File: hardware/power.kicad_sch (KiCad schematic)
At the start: 16 parts

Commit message: MCU module is completed
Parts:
- C1: value (none) -> 10uF/10V; footprint (none) -> Capacitor_SMD:CP_Elec_6.3x7.7
- C2, C6: value (none) -> 100uF/35V; footprint (none) -> Capacitor_SMD:CP_Elec_10x10.5
- C3, C4: value (none) -> 10nF; footprint (none) -> Capacitor_SMD:C_0603_1608Metric
- C5: value (none) -> 10uF/35V; footprint (none) -> Capacitor_SMD:CP_Elec_6.3x7.7
- D1: value (none) -> SBR3A40SAQ; footprint (none) -> Diode_SMD:D_SMB_Handsoldering
- F1: value (none) -> 1A; footprint (none) -> Fuse:Fuse_1206_3216Metric
- R1: value (none) -> 470; footprint (none) -> Resistor_SMD:R_0603_1608Metric
- R2: value (none) -> 18K; footprint (none) -> Resistor_SMD:R_0603_1608Metric
- R3: value (none) -> 10K; footprint (none) -> Resistor_SMD:R_0603_1608Metric
- R4: value (none) -> 1K; footprint (none) -> Resistor_SMD:R_0603_1608Metric
- R5: value (none) -> 33; footprint (none) -> Resistor_SMD:R_0603_1608Metric
- R6: value (none) -> 120; footprint (none) -> Resistor_SMD:R_0603_1608Metric
- U1: value (none) -> TPS7A4901DGNT; footprint (none) -> TPS7A4901DGNT:SOP65P490X110-9N
- U2: value (none) -> LD1085D2M-R; footprint (none) -> LD1085D2MR:LD1085D2M-R
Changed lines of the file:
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@@
       (effects (font (size 1.27 1.27)) (justify left))
     )
-    (property "Value" "" (id 1) (at 128.27 55.88 0)
-      (effects (font (size 1.27 1.27)) (justify left))
-    )
-    (property "Footprint" "" (id 2) (at 127.9652 57.15 0)
+    (property "Value" "100uF/35V" (id 1) (at 128.27 55.88 0)
+      (effects (font (size 1.27 1.27)) (justify left))
+    )
+    (property "Footprint" "Capacitor_SMD:CP_Elec_10x10.5" (id 2) (at 127.9652 57.15 0)
       (effects (font (size 1.27 1.27)) hide)
     )
@@
     (in_bom yes) (on_board yes)
     (property "Reference" "D1" (id 0) (at 115.57 41.91 0))
-    (property "Value" "" (id 1) (at 116.84 46.99 0))
-    (property "Footprint" "" (id 2) (at 115.57 44.45 0)
+    (property "Value" "SBR3A40SAQ" (id 1) (at 116.84 46.99 0))
+    (property "Footprint" "Diode_SMD:D_SMB_Handsoldering" (id 2) (at 115.57 44.45 0)
       (effects (font (size 1.27 1.27)) hide)
     )
@@
     (in_bom yes) (on_board yes)
     (property "Reference" "F1" (id 0) (at 101.6 41.91 90))
-    (property "Value" "" (id 1) (at 101.6 46.99 90))
-    (property "Footprint" "" (id 2) (at 101.6 42.672 90)
+    (property "Value" "1A" (id 1) (at 101.6 46.99 90))
+    (property "Footprint" "Fuse:Fuse_1206_3216Metric" (id 2) (at 101.6 42.672 90)
       (effects (font (size 1.27 1.27)) hide)
     )
@@
       (effects (font (size 1.27 1.27)) (justify left))
     )
-    (property "Value" "" (id 1) (at 199.898 51.943 0)
-      (effects (font (size 1.27 1.27)) (justify left))
-    )
-    (property "Footprint" "" (id 2) (at 196.342 50.8 90)
+    (property "Value" "120" (id 1) (at 199.898 51.943 0)
+      (effects (font (size 1.27 1.27)) (justify left))
+    )
+    (property "Footprint" "Resistor_SMD:R_0603_1608Metric" (id 2) (at 196.342 50.8 90)
       (effects (font (size 1.27 1.27)) hide)
     )
@@
       (effects (font (size 1.27 1.27)) (justify left))
     )
-    (property "Value" "" (id 1) (at 189.738 64.643 0)
-      (effects (font (size 1.27 1.27)) (justify left))
-    )
-    (property "Footprint" "" (id 2) (at 186.182 63.5 90)
+    (property "Value" "1K" (id 1) (at 189.738 64.643 0)
+      (effects (font (size 1.27 1.27)) (justify left))
+    )
+    (property "Footprint" "Resistor_SMD:R_0603_1608Metric" (id 2) (at 186.182 63.5 90)
       (effects (font (size 1.27 1.27)) hide)
     )
@@
       (effects (font (size 1.27 1.27)) (justify left))
     )
-    (property "Value" "" (id 1) (at 210.82 53.34 0)
-      (effects (font (size 1.27 1.27)) (justify left))
-    )
-    (property "Footprint" "" (id 2) (at 211.7852 54.61 0)
+    (property "Value" "100uF/35V" (id 1) (at 210.82 53.34 0)
+      (effects (font (size 1.27 1.27)) (justify left))
+    )
+    (property "Footprint" "Capacitor_SMD:CP_Elec_10x10.5" (id 2) (at 211.7852 54.61 0)
       (effects (font (size 1.27 1.27)) hide)
     )
@@
       (effects (font (size 1.27 1.27)) hide)
     )
-    (property "Value" "" (id 1) (at 188.087 84.4042 0))
+    (property "Value" "GND" (id 1) (at 188.087 84.4042 0))
     (property "Footprint" "" (id 2) (at 187.96 80.01 0)
       (effects (font (size 1.27 1.27)) hide)
@@
     (in_bom yes) (on_board yes)
     (property "Reference" "U1" (id 0) (at 165.1 102.362 0))
-    (property "Value" "" (id 1) (at 165.1 104.6734 0))
-    (property "Footprint" "" (id 2) (at 165.1 119.38 0)
+    (property "Value" "TPS7A4901DGNT" (id 1) (at 165.1 104.6734 0))
+    (property "Footprint" "TPS7A4901DGNT:SOP65P490X110-9N" (id 2) (at 165.1 119.38 0)
       (effects (font (size 1.27 1.27)) (justify left bottom) hide)
     )
@@
       (effects (font (size 1.27 1.27)) (justify left))
     )
-    (property "Value" "" (id 1) (at 142.24 124.46 0)
-      (effects (font (size 1.27 1.27)) (justify left))
-    )
-    (property "Footprint" "" (id 2) (at 141.9352 125.73 0)
+    (property "Value" "10nF" (id 1) (at 142.24 124.46 0)
+      (effects (font (size 1.27 1.27)) (justify left))
+    )
+    (property "Footprint" "Capacitor_SMD:C_0603_1608Metric" (id 2) (at 141.9352 125.73 0)
       (effects (font (size 1.27 1.27)) hide)
     )
@@
       (effects (font (size 1.27 1.27)) (justify left))
     )
-    (property "Value" "" (id 1) (at 204.47 123.19 0)
-      (effects (font (size 1.27 1.27)) (justify left))
-    )
-    (property "Footprint" "" (id 2) (at 204.1652 124.46 0)
+    (property "Value" "10uF/35V" (id 1) (at 204.47 123.19 0)
+      (effects (font (size 1.27 1.27)) (justify left))
+    )
+    (property "Footprint" "Capacitor_SMD:CP_Elec_6.3x7.7" (id 2) (at 204.1652 124.46 0)
       (effects (font (size 1.27 1.27)) hide)
     )
@@
       (effects (font (size 1.27 1.27)) hide)
     )
-    (property "Value" "" (id 1) (at 203.327 132.6642 0))
+    (property "Value" "GND" (id 1) (at 203.327 132.6642 0))
     (property "Footprint" "" (id 2) (at 203.2 128.27 0)
       (effects (font (size 1.27 1.27)) hide)
@@
       (effects (font (size 1.27 1.27)) hide)
     )
-    (property "Value" "" (id 1) (at 185.547 154.2542 0))
+    (property "Value" "GND" (id 1) (at 185.547 154.2542 0))
     (property "Footprint" "" (id 2) (at 185.42 149.86 0)
       (effects (font (size 1.27 1.27)) hide)
@@
       (effects (font (size 1.27 1.27)) hide)
     )
-    (property "Value" "" (id 1) (at 104.521 103.5558 0))
+    (property "Value" "+3V3" (id 1) (at 104.521 103.5558 0))
     (property "Footprint" "" (id 2) (at 104.14 107.95 0)
       (effects (font (size 1.27 1.27)) hide)
@@
       (effects (font (size 1.27 1.27)) (justify left))
     )
-    (property "Value" "" (id 1) (at 132.08 124.46 0)
-      (effects (font (size 1.27 1.27)) (justify left))
-    )
-    (property "Footprint" "" (id 2) (at 131.7752 125.73 0)
+    (property "Value" "10nF" (id 1) (at 132.08 124.46 0)
+      (effects (font (size 1.27 1.27)) (justify left))
+    )
+    (property "Footprint" "Capacitor_SMD:C_0603_1608Metric" (id 2) (at 131.7752 125.73 0)
       (effects (font (size 1.27 1.27)) hide)
     )
@@
       (effects (font (size 1.27 1.27)) (justify left))
     )
-    (property "Value" "" (id 1) (at 118.618 123.063 0)
-      (effects (font (size 1.27 1.27)) (justify left))
-    )
-    (property "Footprint" "" (id 2) (at 115.062 121.92 90)
+    (property "Value" "18K" (id 1) (at 118.618 123.063 0)
+      (effects (font (size 1.27 1.27)) (justify left))
+    )
+    (property "Footprint" "Resistor_SMD:R_0603_1608Metric" (id 2) (at 115.062 121.92 90)
       (effects (font (size 1.27 1.27)) hide)
     )
@@
       (effects (font (size 1.27 1.27)) (justify left))
     )
-    (property "Value" "" (id 1) (at 118.618 139.573 0)
-      (effects (font (size 1.27 1.27)) (justify left))
-    )
-    (property "Footprint" "" (id 2) (at 115.062 138.43 90)
+    (property "Value" "10K" (id 1) (at 118.618 139.573 0)
+      (effects (font (size 1.27 1.27)) (justify left))
+    )
+    (property "Footprint" "Resistor_SMD:R_0603_1608Metric" (id 2) (at 115.062 138.43 90)
       (effects (font (size 1.27 1.27)) hide)
     )
@@
       (effects (font (size 1.27 1.27)) (justify left))
     )
-    (property "Value" "" (id 1) (at 105.41 132.08 0)
-      (effects (font (size 1.27 1.27)) (justify left))
-    )
-    (property "Footprint" "" (id 2) (at 105.1052 133.35 0)
+    (property "Value" "10uF/10V" (id 1) (at 105.41 132.08 0)
+      (effects (font (size 1.27 1.27)) (justify left))
+    )
+    (property "Footprint" "Capacitor_SMD:CP_Elec_6.3x7.7" (id 2) (at 105.1052 133.35 0)
       (effects (font (size 1.27 1.27)) hide)
     )
@@
       (effects (font (size 1.27 1.27)) hide)
     )
-    (property "Value" "" (id 1) (at 127.127 66.6242 0))
+    (property "Value" "GND" (id 1) (at 127.127 66.6242 0))
     (property "Footprint" "" (id 2) (at 127 62.23 0)
       (effects (font (size 1.27 1.27)) hide)
@@
       (effects (font (size 1.27 1.27)) hide)
     )
-    (property "Value" "" (id 1) (at 226.441 32.4358 0))
+    (property "Value" "+12V" (id 1) (at 226.441 32.4358 0))
     (property "Footprint" "" (id 2) (at 226.06 36.83 0)
       (effects (font (size 1.27 1.27)) hide)
@@
       (effects (font (size 1.27 1.27)) hide)
     )
-    (property "Value" "" (id 1) (at 91.821 32.4358 0))
+    (property "Value" "VCC" (id 1) (at 91.821 32.4358 0))
     (property "Footprint" "" (id 2) (at 91.44 36.83 0)
       (effects (font (size 1.27 1.27)) hide)
@@
       (effects (font (size 1.524 1.524)))
     )
-    (property "Value" "" (id 1) (at 157.48 52.07 0)
+    (property "Value" "LD1085D2M-R" (id 1) (at 157.48 52.07 0)
       (effects (font (size 1.524 1.524)))
     )
-    (property "Footprint" "" (id 2) (at 157.48 35.814 0)
+    (property "Footprint" "LD1085D2MR:LD1085D2M-R" (id 2) (at 157.48 35.814 0)
       (effects (font (size 1.524 1.524)) hide)
     )
@@
       (effects (font (size 1.27 1.27)) hide)
     )
-    (property "Value" "" (id 1) (at 210.947 64.0842 0))
+    (property "Value" "GND" (id 1) (at 210.947 64.0842 0))
     (property "Footprint" "" (id 2) (at 210.82 59.69 0)
       (effects (font (size 1.27 1.27)) hide)
@@
       (effects (font (size 1.27 1.27)) (justify left))
     )
-    (property "Value" "" (id 1) (at 189.738 74.803 0)
-      (effects (font (size 1.27 1.27)) (justify left))
-    )
-    (property "Footprint" "" (id 2) (at 186.182 73.66 90)
+    (property "Value" "33" (id 1) (at 189.738 74.803 0)
+      (effects (font (size 1.27 1.27)) (justify left))
+    )
+    (property "Footprint" "Resistor_SMD:R_0603_1608Metric" (id 2) (at 186.182 73.66 90)
       (effects (font (size 1.27 1.27)) hide)
     )
@@
     (in_bom yes) (on_board yes)
     (property "Reference" "R1" (id 0) (at 97.79 109.22 90))
-    (property "Value" "" (id 1) (at 97.79 114.3 90))
-    (property "Footprint" "" (id 2) (at 97.79 109.982 90)
-      (effects (font (size 1.27 1.27)) hide)
-    )
+    (property "Value" "470" (id 1) (at 97.79 114.3 90))
+    (property "Footprint" "Resistor_SMD:R_0603_1608Metric" (id 2) (at 97.79 109.982 90)
+      (effects (font (size 1.27 1.27)) hide)
+    )

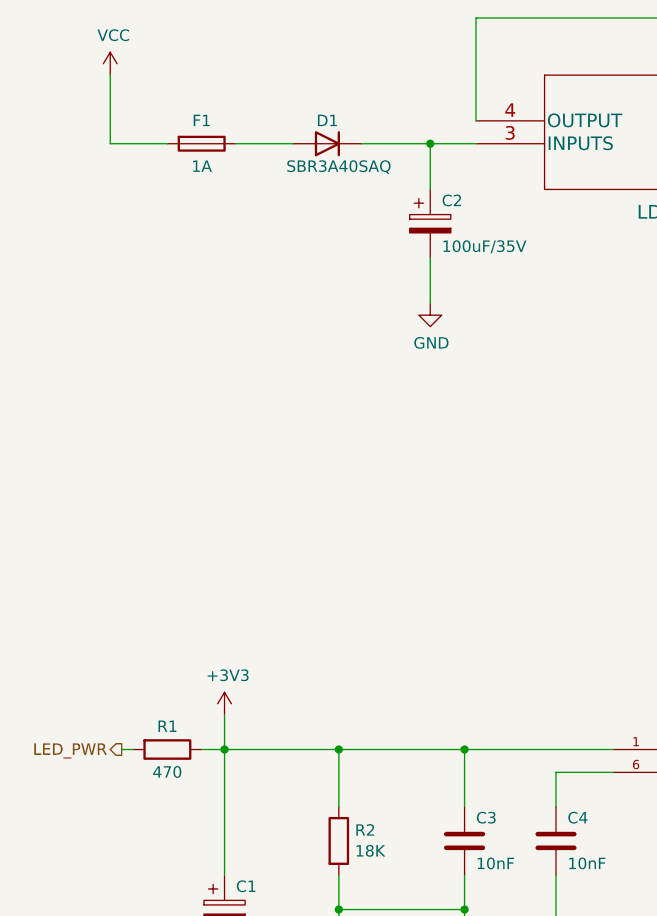
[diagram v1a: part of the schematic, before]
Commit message: Relay module completed
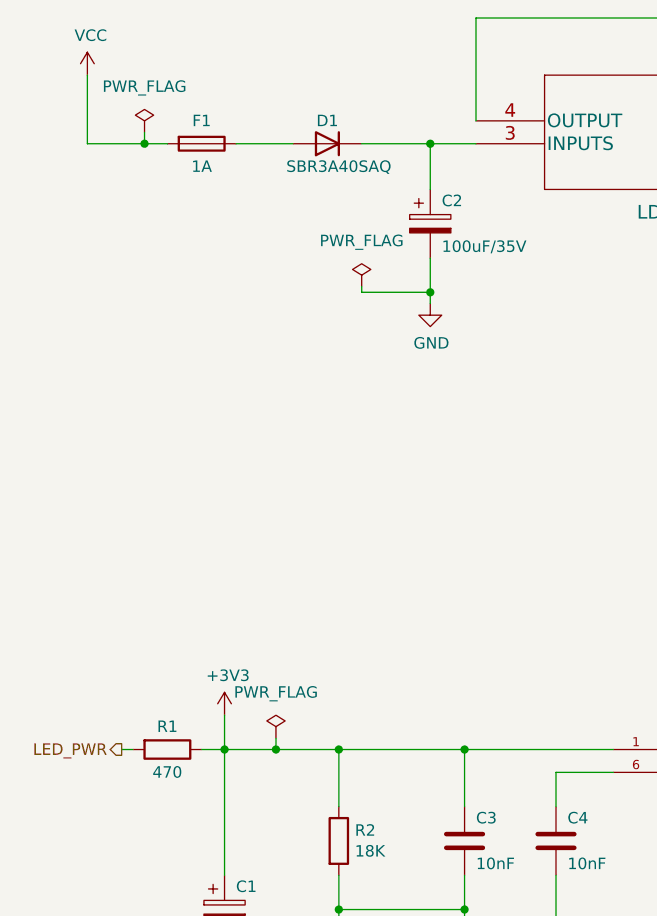
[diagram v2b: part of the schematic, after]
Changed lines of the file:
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@@
   (junction (at 203.2 111.76) (diameter 0) (color 0 0 0 0)
   )
+  (junction (at 95.25 44.45) (diameter 0) (color 0 0 0 0)
+  )
   (junction (at 185.42 111.76) (diameter 0) (color 0 0 0 0)
   )
@@
   (junction (at 104.14 111.76) (diameter 0) (color 0 0 0 0)
   )
+  (junction (at 109.855 111.76) (diameter 0) (color 0 0 0 0)
+  )
   (junction (at 140.97 147.32) (diameter 0) (color 0 0 0 0)
   )
@@
   (junction (at 116.84 111.76) (diameter 0) (color 0 0 0 0)
   )
+  (junction (at 127 60.96) (diameter 0) (color 0 0 0 0)
+  )
   (junction (at 198.12 44.45) (diameter 0) (color 0 0 0 0)
   )
@@
     (stroke (width 0) (type default) (color 0 0 0 0))
   )
-  (wire (pts (xy 127 62.23) (xy 127 57.15))
+  (wire (pts (xy 127 62.23) (xy 127 60.96))
     (stroke (width 0) (type default) (color 0 0 0 0))
   )
@@
     (stroke (width 0) (type default) (color 0 0 0 0))
   )
-  (wire (pts (xy 104.14 111.76) (xy 116.84 111.76))
+  (wire (pts (xy 104.14 111.76) (xy 109.855 111.76))
     (stroke (width 0) (type default) (color 0 0 0 0))
   )
@@
     (stroke (width 0) (type default) (color 0 0 0 0))
   )
+  (wire (pts (xy 119.38 60.325) (xy 119.38 60.96))
+    (stroke (width 0) (type default) (color 0 0 0 0))
+  )
   (wire (pts (xy 140.97 125.73) (xy 140.97 147.32))
     (stroke (width 0) (type default) (color 0 0 0 0))
@@
     (stroke (width 0) (type default) (color 0 0 0 0))
   )
+  (wire (pts (xy 95.25 43.18) (xy 95.25 44.45))
+    (stroke (width 0) (type default) (color 0 0 0 0))
+  )
   (wire (pts (xy 185.42 147.32) (xy 185.42 149.86))
     (stroke (width 0) (type default) (color 0 0 0 0))
@@
     (stroke (width 0) (type default) (color 0 0 0 0))
   )
+  (wire (pts (xy 95.25 44.45) (xy 97.79 44.45))
+    (stroke (width 0) (type default) (color 0 0 0 0))
+  )
   (wire (pts (xy 226.06 111.76) (xy 203.2 111.76))
     (stroke (width 0) (type default) (color 0 0 0 0))
   )
-  (wire (pts (xy 91.44 36.83) (xy 91.44 44.45))
+  (wire (pts (xy 88.9 36.83) (xy 88.9 44.45))
     (stroke (width 0) (type default) (color 0 0 0 0))
   )
@@
     (stroke (width 0) (type default) (color 0 0 0 0))
   )
-  (wire (pts (xy 91.44 44.45) (xy 97.79 44.45))
+  (wire (pts (xy 88.9 44.45) (xy 95.25 44.45))
     (stroke (width 0) (type default) (color 0 0 0 0))
   )
@@
     (stroke (width 0) (type default) (color 0 0 0 0))
   )
+  (wire (pts (xy 127 60.96) (xy 127 57.15))
+    (stroke (width 0) (type default) (color 0 0 0 0))
+  )
   (wire (pts (xy 210.82 54.61) (xy 210.82 59.69))
     (stroke (width 0) (type default) (color 0 0 0 0))
@@
     (stroke (width 0) (type default) (color 0 0 0 0))
   )
+  (wire (pts (xy 109.855 111.76) (xy 116.84 111.76))
+    (stroke (width 0) (type default) (color 0 0 0 0))
+  )
   (wire (pts (xy 187.96 77.47) (xy 187.96 80.01))
     (stroke (width 0) (type default) (color 0 0 0 0))
@@
     (stroke (width 0) (type default) (color 0 0 0 0))
   )
+  (wire (pts (xy 119.38 60.96) (xy 127 60.96))
+    (stroke (width 0) (type default) (color 0 0 0 0))
+  )
   (wire (pts (xy 187.96 67.31) (xy 187.96 69.85))
+    (stroke (width 0) (type default) (color 0 0 0 0))
+  )
+  (wire (pts (xy 109.855 110.49) (xy 109.855 111.76))
     (stroke (width 0) (type default) (color 0 0 0 0))
   )
@@
     (pin "1")
   )
-  (symbol (lib_id "power:VCC") (at 91.44 36.83 0) (unit 1)
-    (in_bom yes) (on_board yes)
-    (property "Reference" "#PWR011" (id 0) (at 91.44 40.64 0)
-      (effects (font (size 1.27 1.27)) hide)
-    )
-    (property "Value" "VCC" (id 1) (at 91.821 32.4358 0))
-    (property "Footprint" "" (id 2) (at 91.44 36.83 0)
-      (effects (font (size 1.27 1.27)) hide)
-    )
-    (property "Datasheet" "" (id 3) (at 91.44 36.83 0)
+  (symbol (lib_id "power:VCC") (at 88.9 36.83 0) (unit 1)
+    (in_bom yes) (on_board yes)
+    (property "Reference" "#PWR011" (id 0) (at 88.9 40.64 0)
+      (effects (font (size 1.27 1.27)) hide)
+    )
+    (property "Value" "VCC" (id 1) (at 89.281 32.4358 0))
+    (property "Footprint" "" (id 2) (at 88.9 36.83 0)
+      (effects (font (size 1.27 1.27)) hide)
+    )
+    (property "Datasheet" "" (id 3) (at 88.9 36.83 0)
       (effects (font (size 1.27 1.27)) hide)
     )
@@
     (pin "2")
   )
+  (symbol (lib_id "power:PWR_FLAG") (at 109.855 110.49 0) (unit 1)
+    (in_bom yes) (on_board yes) (fields_autoplaced)
+    (property "Reference" "#FLG?" (id 0) (at 109.855 108.585 0)
+      (effects (font (size 1.27 1.27)) hide)
+    )
+    (property "Value" "PWR_FLAG" (id 1) (at 109.855 105.41 0))
+    (property "Footprint" "" (id 2) (at 109.855 110.49 0)
+      (effects (font (size 1.27 1.27)) hide)
+    )
+    (property "Datasheet" "~" (id 3) (at 109.855 110.49 0)
+      (effects (font (size 1.27 1.27)) hide)
+    )
+    (pin "1")
+  )
+  (symbol (lib_id "power:PWR_FLAG") (at 119.38 60.325 0) (unit 1)
+    (in_bom yes) (on_board yes) (fields_autoplaced)
+    (property "Reference" "#FLG?" (id 0) (at 119.38 58.42 0)
+      (effects (font (size 1.27 1.27)) hide)
+    )
+    (property "Value" "PWR_FLAG" (id 1) (at 119.38 55.245 0))
+    (property "Footprint" "" (id 2) (at 119.38 60.325 0)
+      (effects (font (size 1.27 1.27)) hide)
+    )
+    (property "Datasheet" "~" (id 3) (at 119.38 60.325 0)
+      (effects (font (size 1.27 1.27)) hide)
+    )
+    (pin "1")
+  )
+  (symbol (lib_id "power:PWR_FLAG") (at 95.25 43.18 0) (unit 1)
+    (in_bom yes) (on_board yes) (fields_autoplaced)
+    (property "Reference" "#FLG?" (id 0) (at 95.25 41.275 0)
+      (effects (font (size 1.27 1.27)) hide)
+    )
+    (property "Value" "PWR_FLAG" (id 1) (at 95.25 38.1 0))
+    (property "Footprint" "" (id 2) (at 95.25 43.18 0)
+      (effects (font (size 1.27 1.27)) hide)
+    )
+    (property "Datasheet" "~" (id 3) (at 95.25 43.18 0)
+      (effects (font (size 1.27 1.27)) hide)
+    )
+    (pin "1")
+  )
 )
